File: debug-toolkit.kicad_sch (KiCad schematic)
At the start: 130 parts, among them J1 USB-C_USB4105-GF-A, J2 PinHeader_Shrouded_2x5_P2mm_D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, J3 PinHeader_2x8_P2.54mm_Drill1mm, J4 PinHeader_1x2_P2.54mm_Drill1.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, J5 PinHeader_1x2_P1.27mm_Drill0.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, J6 PinHeader_1x4_P2.54mm_Drill1.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, Q1 NX3008CBKV, Q2 NX3008CBKV, Q3 BC807-25W, Q4 SSM3K15ACT, Q5 SSM3K15ACT, Q6 SSM3K15ACT, Q7 SSM3K15ACT, SW1_A1 PinHeader_1x3_P2.54mm_Drill1.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, SW1_B1 PinHeader_1x3_P2.54mm_Drill1.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, SW2 PinHeader_2x3_P2.54mm_Drill1mm, U1 FT4232H_VQFN, U10 74LVC2T45_SOT833, U11 NTS0302JKZ, U12 TLV70033_SC70, U13 74HC00_DHVQFN, U14 TLV70018_SC70, U15 TS5A3359_VSSOP, U16 TS5A3359_VSSOP, U2 SN74LVC1T45_SOT-5X3, U3 SN74LVC1T45_SOT-5X3, U4 TXB0104_UQFN, U5 74LVC2T45_SOT833, U6 74LVC2T45_SOT833, U7 74LVC2T45_SOT833, U8 SN74LVC1T45_SOT-5X3, U9 SN74LVC1T45_SOT-5X3, Y1 Oscillator_SMD_12MHz_ASFLMB

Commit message: Bump revision, change name on PCB and in schematics
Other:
- title: FTDI Toolkit -> Debug Toolkit
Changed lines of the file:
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@@
   (paper "A2")
   (title_block
-    (title "FTDI Toolkit")
+    (title "Debug Toolkit")
     (date "2022-08-03")
-    (rev "1.3.6")
+    (rev "1.3.8")
     (comment 1 "www.antmicro.com")
     (comment 2 "Antmicro Ltd.")

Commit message: [#57618] Perform globlib
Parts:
- 1V8_A1, 1V8_B1, 3V3_A1, 3V3_B1, 5V0_A1, 5V0_B1, RX_A1, RX_B1, TX_A1, TX_B1, USB1: footprint debug-toolkit-footprints:LED_0603_1608Metric_G -> antmicro-footprints:LED_0603_1608Metric_G; symbol debug-toolkit:LED_G_0603_LG_L29K-G2J1-24-Z -> antmicroLEDIndicationDiscrete:LED_G_0603_LG_L29K-G2J1-24-Z
- C1, C2, C36, C5, C6: footprint debug-toolkit-footprints:C_0603_1608Metric -> antmicro-footprints:C_0603_1608Metric; symbol debug-toolkit:C_1u_0603 -> antmicroCapacitors0603:C_1u_0603
- C11, C23, C27, C33: footprint debug-toolkit-footprints:C_0402_1005Metric -> antmicro-footprints:C_0402_1005Metric; symbol debug-toolkit:C_4u7_0402 -> antmicroCapacitors0402:C_4u7_0402
- C3: footprint debug-toolkit-footprints:C_0402_1005Metric -> antmicro-footprints:C_0402_1005Metric; symbol debug-toolkit:C_10n_0402 -> antmicroCapacitors0402:C_10n_0402
- D1: footprint debug-toolkit-footprints:SOT-723 -> antmicro-footprints:SOT-723; symbol debug-toolkit:TPD2E009_SOT-9X3 -> antmicroTVSDiodes:TPD2E009_SOT-9X3
- D2: footprint debug-toolkit-footprints:USON-14_3.5X1.3X0.5mm_P0.5mm -> antmicro-footprints:USON-14_3.5X1.3X0.5mm_P0.5mm; symbol debug-toolkit:TPD6E05U06RVZR -> antmicroTVSDiodes:TPD6E05U06RVZR
- D3, D4: footprint debug-toolkit-footprints:SOD-523 -> antmicro-footprints:SOD-523; symbol debug-toolkit:BAT54-02V-G3-08 -> antmicroDiodesRectifiersSingle:BAT54-02V-G3-08
- FB1, FB2: footprint debug-toolkit-footprints:FB_0402_1005Metric -> antmicro-footprints:FB_0402_1005Metric; symbol debug-toolkit:FB_600Z_0.3A_0402 -> antmicroFerriteBeadsandChips:FB_600Z_0.3A_Murata-BLM15AG_0402
- J1: footprint debug-toolkit-footprints:GCT_USB4105-GF-A -> antmicro-footprints:USB-C_Receptacle_GCT_USB4105-GF-A; symbol debug-toolkit:USB-C_USB4105-GF-A -> antmicroUSBConnectors:USB-C_GCT_USB4105-GF-A
- J2: footprint debug-toolkit-footprints:IDC-Header_2x05_P1.27_Vertical_SMD_Samtec_SHF-105-01-X-D-SM -> antmicro-footprints:PinHeader_2x5_P1.27mm_SMD_Shrouded; symbol debug-toolkit:PinHeader_Shrouded_2x5_P2mm_Drill0.71mm -> antmicroGenericPinHeaders:PinHeader_2x5_P1.27mm_SMD_Shrouded
- J3: footprint debug-toolkit-footprints:PinHeader_2x8_P2.54mm_Drill1mm -> antmicro-footprints:PinHeader_2x8_P2.54mm_Drill1mm; symbol debug-toolkit:PinHeader_2x8_P2.54mm_Drill1mm -> antmicroGenericPinHeaders:PinHeader_2x8_P2.54mm_Drill1mm
- J4: footprint debug-toolkit-footprints:PinHeader_1x2_P2.54mm_Drill1.02mm -> antmicro-footprints:PinHeader_1x2_P2.54mm_Drill1.02mm; symbol debug-toolkit:PinHeader_1x2_P2.54mm_Drill1.02mm -> antmicroGenericPinHeaders:PinHeader_1x2_P2.54mm_Drill1.02mm
- J5: footprint debug-toolkit-footprints:PinHeader_1x2_P1.27mm_Drill0.7mm -> antmicro-footprints:PinHeader_1x2_P1.27mm_Drill0.7mm; symbol debug-toolkit:PinHeader_1x2_P1.27mm_Drill0.7mm -> antmicroGenericPinHeaders:PinHeader_1x2_P1.27mm_Drill0.7mm
- J6: footprint debug-toolkit-footprints:PinHeader_1x4_P2.54mm_Drill1.02mm -> antmicro-footprints:PinHeader_1x4_P2.54mm_Drill1.1mm; symbol debug-toolkit:PinHeader_1x4_P2.54mm_Drill1.1mm -> antmicroGenericPinHeaders:PinHeader_1x4_P2.54mm_Drill1.1mm
- L1, L2: footprint debug-toolkit-footprints:FB_0603_1608Metric -> antmicro-footprints:FB_0603_1608Metric; symbol debug-toolkit:FB_120Z_2A_0603 -> antmicroFerriteBeadsandChips:FB_120Z_2A_Murata-BLM18PG_0603
- N1: footprint debug-toolkit-footprints:antmicro-logo_scaled_12mm -> antmicro-footprints:antmicro-logo; symbol debug-toolkit:antmicro_logo -> antmicroMechanicalParts:antmicro_logo
- N2: footprint debug-toolkit-footprints:oshw-logo -> antmicro-footprints:oshw-logo; symbol debug-toolkit:oshw_logo -> antmicroMechanicalParts:oshw_logo
- Q1, Q2: footprint debug-toolkit-footprints:SOT-666 -> antmicro-footprints:SOT-666; symbol debug-toolkit:NX3008CBKV -> antmicroTransistorsFETsMOSFETsArrays:NX3008CBKV
- Q3: footprint debug-toolkit-footprints:SOT-323 -> antmicro-footprints:SOT-323; symbol debug-toolkit:BC807-25W -> antmicroTransistorsBipolarSingle:BC807-25W
- Q4, Q5, Q6, Q7: footprint debug-toolkit-footprints:CST3-3 -> antmicro-footprints:CST3-3; symbol debug-toolkit:SSM3K15ACT -> antmicroTransistorsFETsMOSFETsSingle:SSM3K15ACT
- R1, R11, R12, R13, R14, R15, R18, R3, R34, R35, R36, R6, R7, R8: footprint debug-toolkit-footprints:R_0402_1005Metric -> antmicro-footprints:R_0402_1005Metric; symbol debug-toolkit:R_220R_0402 -> antmicroResistors0402:R_220R_0402
- R10, R31, R37, R38: footprint debug-toolkit-footprints:R_0201 -> antmicro-footprints:R_0201; symbol debug-toolkit:R_100k_0201 -> antmicroResistorsmisc:R_100k_0201
- R16, R17, R22, R25, R26, R27, R30, R32, R33, R4, R5: footprint debug-toolkit-footprints:R_0402_1005Metric -> antmicro-footprints:R_0402_1005Metric; symbol debug-toolkit:R_10k_0402 -> antmicroResistors0402:R_10k_0402
- R19, R28: footprint debug-toolkit-footprints:R_0402_1005Metric -> antmicro-footprints:R_0402_1005Metric; symbol debug-toolkit:R_510R_0402 -> antmicroResistors0402:R_510R_0402
- R2: footprint debug-toolkit-footprints:R_0402_1005Metric -> antmicro-footprints:R_0402_1005Metric; symbol debug-toolkit:R_470R_0402 -> antmicroResistors0402:R_470R_0402
- R20, R24: footprint debug-toolkit-footprints:R_0402_1005Metric -> antmicro-footprints:R_0402_1005Metric; symbol debug-toolkit:R_1k_0402 -> antmicroResistors0402:R_1k_0402
- R21: footprint debug-toolkit-footprints:R_0402_1005Metric -> antmicro-footprints:R_0402_1005Metric; symbol debug-toolkit:R_4k7_0402 -> antmicroResistors0402:R_4k7_0402
- R23, R29: footprint debug-toolkit-footprints:R_0402_1005Metric -> antmicro-footprints:R_0402_1005Metric; symbol debug-toolkit:R_56k_0402 -> antmicroResistors0402:R_56k_0402
- R9: footprint debug-toolkit-footprints:R_0402_1005Metric -> antmicro-footprints:R_0402_1005Metric; symbol debug-toolkit:R_12k_0402 -> antmicroResistors0402:R_12k_0402
- SW1_A1, SW1_B1: footprint debug-toolkit-footprints:PinHeader_1x3_P2.54_Drill1.1mm -> antmicro-footprints:PinHeader_1x3_P2.54mm_Drill1.1mm; symbol debug-toolkit:PinHeader_1x3_P2.54mm_Drill1.1mm -> antmicroGenericPinHeaders:PinHeader_1x3_P2.54mm_Drill1.1mm
- SW2: footprint debug-toolkit-footprints:PinHeader_2x3_P2.54mm_Drill1mm -> antmicro-footprints:PinHeader_2x3_P2.54mm_Drill1.1mm; symbol debug-toolkit:PinHeader_2x3_P2.54mm_Drill1mm -> antmicroGenericPinHeaders:PinHeader_2x3_P2.54mm_Drill1.1mm
- U1: footprint debug-toolkit-footprints:QFN-56-1EP_8x8mm_P0.5mm -> antmicro-footprints:QFN-56-1EP_8x8mm_P0.5mm; symbol debug-toolkit:FT4232H_VQFN -> antmicroInterfaceControllers:FT4232H_VQFN
- U10, U5, U6, U7: footprint debug-toolkit-footprints:XSON-8_1x1.95mm_P0.5mm -> antmicro-footprints:XSON-8_1x1.95mm_P0.5mm; symbol debug-toolkit:74LVC2T45_SOT833 -> antmicroLogicTranslatorsLevelShifters:74LVC2T45_SOT833
- U11: footprint debug-toolkit-footprints:X2SON8_1.4x1x0.32mm_P0.35mm -> antmicro-footprints:X2SON8_1.4x1x0.32mm_P0.35mm; symbol debug-toolkit:NTS0302JKZ -> antmicroLogicTranslatorsLevelShifters:NTS0302JKZ
- U12: footprint debug-toolkit-footprints:SC-70-5 -> antmicro-footprints:SC-70-5; symbol debug-toolkit:TLV70033_SC70 -> antmicroPMICVoltageRegulatorsLinear:TLV70033_SC70
- U13: footprint debug-toolkit-footprints:DHVQFN-14_1EP_2.5x3mm -> antmicro-footprints:DHVQFN-14-1EP_2.5x3mm; symbol debug-toolkit:74HC00_DHVQFN -> antmicroLogicGatesandInverters:74HC00_DHVQFN
- U14: footprint debug-toolkit-footprints:SC-70-5 -> antmicro-footprints:SC-70-5; symbol debug-toolkit:TLV70018_SC70 -> antmicroPMICVoltageRegulatorsLinear:TLV70018_SC70
- U15, U16: footprint debug-toolkit-footprints:VSSOP-8_2.3x2mm_P0.5mm -> antmicro-footprints:VSSOP-8_2.3x2mm_P0.5mm; symbol debug-toolkit:TS5A3359_VSSOP -> antmicroInterfaceAnalogSwitchesMultiplexersDemultiplexers:TS5A3359_VSSOP
- U2, U3, U8, U9: footprint debug-toolkit-footprints:SOT-553-6 -> antmicro-footprints:SOT-553-6; symbol debug-toolkit:SN74LVC1T45_SOT-5X3 -> antmicroLogicTranslatorsLevelShifters:SN74LVC1T45_SOT-5X3
- U4: footprint debug-toolkit-footprints:UQFN-12_2x1.7mm_P0.4mm_Texas_RUT -> antmicro-footprints:UQFN-12_2x1.7mm_P0.4mm_Texas_RUT; symbol debug-toolkit:TXB0104_UQFN -> antmicroLogicTranslatorsLevelShifters:TXB0104_UQFN
- Y1: footprint debug-toolkit-footprints:Oscillator_SMD_Abracon_ASFLMB_5x3.2x0.85mm -> antmicro-footprints:Oscillator_SMD_Abracon_ASFLMB_5x3.2x0.85mm; symbol debug-toolkit:Oscillator_SMD_12MHz_ASFLMB -> antmicroOscillators:Oscillator_12MHz_ASFLMB

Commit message: [#57618] Update symbols from global lib
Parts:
- 1V8_A1, 1V8_B1, 3V3_A1, 3V3_B1, 5V0_A1, 5V0_B1, RX_A1, RX_B1, TX_A1, TX_B1, USB1: Color (none) -> Green; Manufacturer Osram -> OSRAM
- FB1, FB2: value FB_600Z_0.3A_0402 -> FB_600Z_0.3A_Murata-BLM15AG_0402; Val (none) -> 600Z/0.3A
- J1: value USB-C_USB4105-GF-A -> USB-C_GCT_USB4105-GF-A; VSD_Class (none) -> USB-C
- J2: value PinHeader_Shrouded_2x5_P2mm_Drill0.71mm -> PinHeader_2x5_P1.27mm_SMD_Shrouded
- J3: Manufacturer Wurth -> Würth Elektronik
- J4: Manufacturer Harwin -> Molex
- J5: Manufacturer Multicomp -> Multicomp Pro
- L1, L2: value FB_120Z_2A_0603 -> FB_120Z_2A_Murata-BLM18PG_0603; Val (none) -> 120Z/2A
- N1, N2: Manufacturer None -> (none); now left out of the parts list
- Q3: MPN SBC807-25WT1G -> SBC807-40WT1G
- Q4, Q5, Q6, Q7: MPN SSM3K15ACT,L3F -> SSM3K15ACT,L3F
- SW1_A1, SW1_B1: VSD_class (none) -> IO Header
- SW2: value PinHeader_2x3_P2.54mm_Drill1mm -> PinHeader_2x3_P2.54mm_Drill1.1mm; Manufacturer Wurth -> Würth Elektronik
- U1: Manufacturer FTDI -> FTDI Chip
- Y1: value Oscillator_SMD_12MHz_ASFLMB -> Oscillator_12MHz_ASFLMB; Val (none) -> 12 MHz
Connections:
- net 3V3_FT: now also SW2.3, SW2.4; no longer SW2.2, SW2.5
- net MPSSE_B: now also SW2.5; no longer SW2.3
- net SWD_EN: now also SW2.2; no longer SW2.4
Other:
- moved on the sheet: 1V8_A1, 1V8_B1, 3V3_A1, 3V3_B1, 5V0_A1, 5V0_B1, C1, C10, C11, C12, C13, C14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

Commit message: [#57618] Update C_100n_16V_0402 to global lib
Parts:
- C10, C12, C13, C14, C15, C16, C17, C18, C19, C20, C21, C22, C24, C25, C26, C28, C29, C30, C31, C32, C34, C35, C4, C7, C8, C9: value C_100n_16V_0402 -> C_100n_16V_X7R_0402; footprint debug-toolkit-footprints:C_0402_1005Metric -> antmicro-footprints:C_0402_1005Metric; symbol debug-toolkit:C_100n_16V_0402 -> antmicroCapacitors0402:C_100n_16V_X7R_0402; Dielectric (none) -> X7R; MPN MC0402B104K160CT -> C0402C104J4RAC7411; Manufacturer Multicomp -> KEMET; Voltage (none) -> 16V

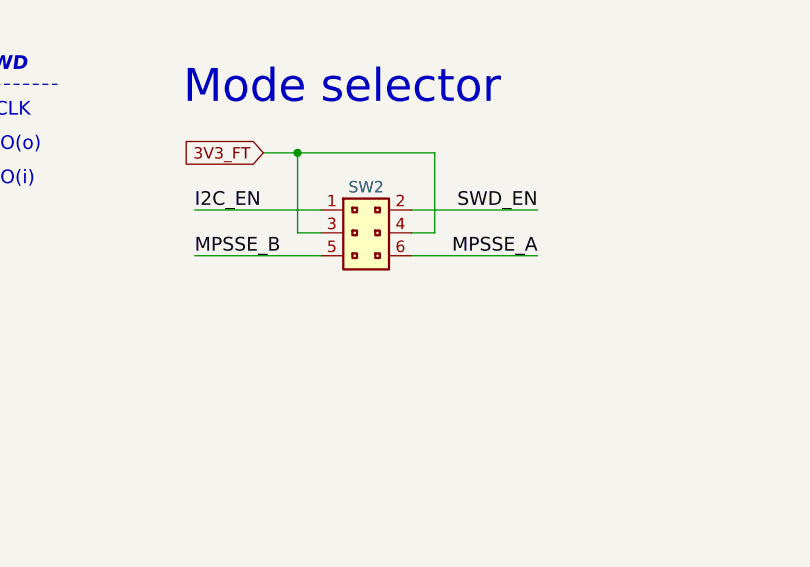
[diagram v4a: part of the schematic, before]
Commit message: [#57618] Update SW2 diameter and MPN
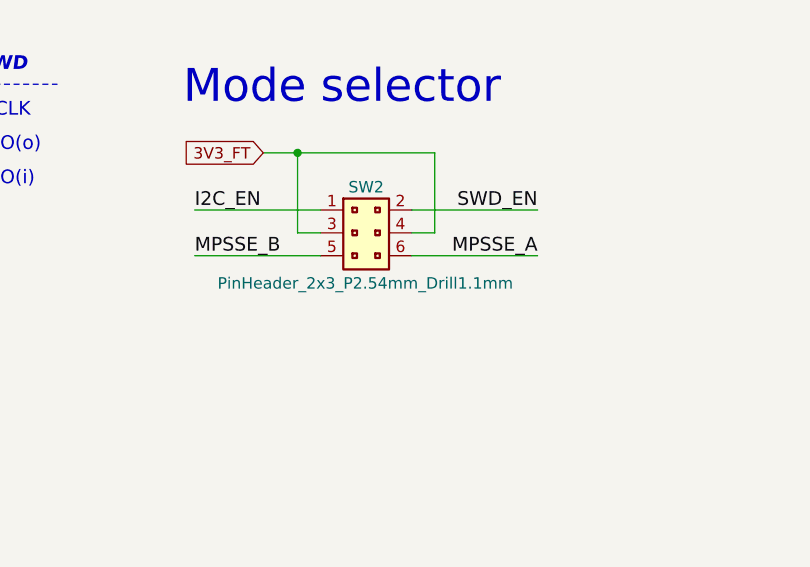
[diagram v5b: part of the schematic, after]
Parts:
- SW2: MPN 61000621121 -> 61300621121
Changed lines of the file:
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@@
       (effects (font (size 1.27 1.27) (thickness 0.15)))
     )
-    (property "Value" "PinHeader_2x3_P2.54mm_Drill1.1mm" (at 173.99 341.63 0)
-      (effects (font (size 1.27 1.27) (thickness 0.15)) (justify left bottom) hide)
+    (property "Value" "PinHeader_2x3_P2.54mm_Drill1.1mm" (at 137.16 342.9 0)
+      (effects (font (size 1.27 1.27) (thickness 0.15)) (justify left bottom))
     )
     (property "Footprint" "antmicro-footprints:PinHeader_2x3_P2.54mm_Drill1.1mm" (at 173.99 344.17 0)
@@
       (effects (font (size 1.27 1.27) (thickness 0.15)) (justify left bottom) hide)
     )
-    (property "MPN" "61000621121" (at 173.99 351.79 0)
+    (property "MPN" "61300621121" (at 173.99 351.79 0)
       (effects (font (size 1.27 1.27) (thickness 0.15)) (justify left bottom) hide)
     )

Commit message: [#57618] Update symbols
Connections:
- net 3V3_FT: now also D3.2 (A); no longer D3.1
- net SDA: now also D4.1 (C); no longer D4.2
- net at C33.2, R34.1, U11.1 (VCC_A): now also D3.1 (C); no longer D3.2
- net at U7.7 (1B): now also D4.2 (A); no longer D4.1
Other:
- moved on the sheet: R10, R31, R37, R38

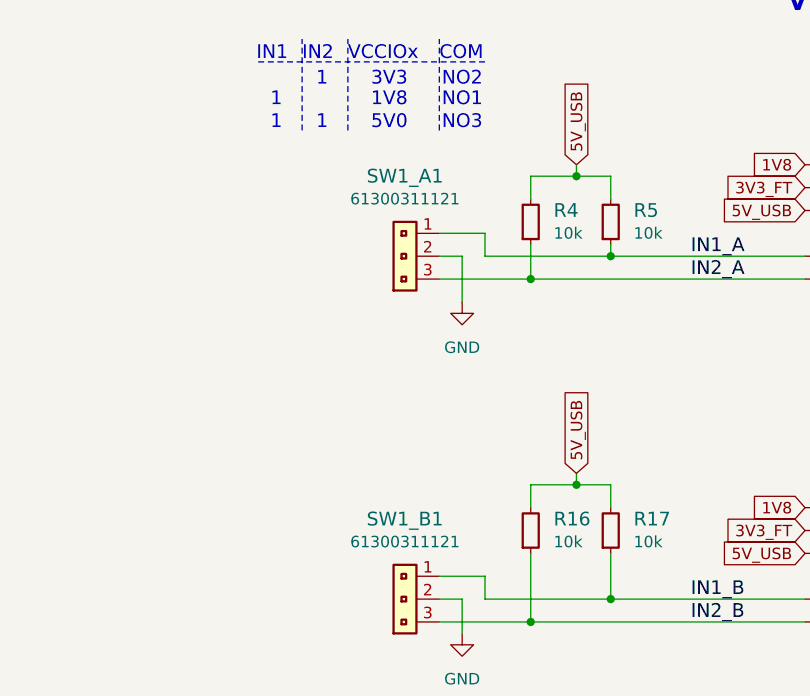
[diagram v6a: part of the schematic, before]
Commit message: Rename SW1 to J1
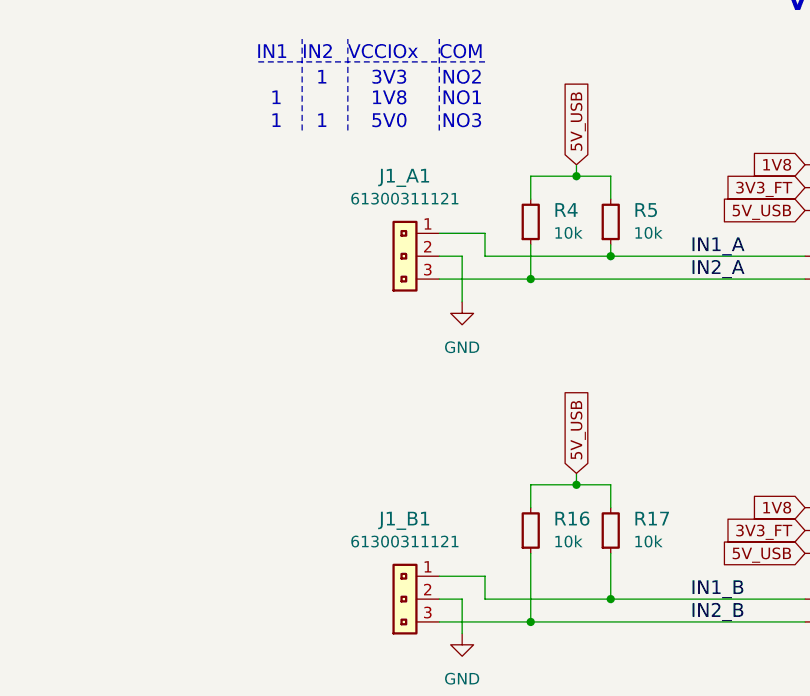
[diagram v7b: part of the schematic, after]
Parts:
- renumbered SW1_A1 to J1_A1, SW1_B1 to J1_B1
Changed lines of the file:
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@@
   (symbol (lib_id "antmicroGenericPinHeaders:PinHeader_1x3_P2.54mm_Drill1.1mm") (at 309.88 91.44 0) (mirror y) (unit 1)
     (in_bom yes) (on_board yes) (dnp no) (fields_autoplaced)
-    (property "Reference" "SW1_B1" (at 306.07 85.09 0)
+    (property "Reference" "J1_B1" (at 306.07 85.09 0)
       (effects (font (size 1.524 1.524)))
     )
@@
       (project "debug-toolkit"
         (path "/dd9af27c-a67f-40d3-942b-1892dec86b34"
-          (reference "SW1_B1") (unit 1)
+          (reference "J1_B1") (unit 1)
         )
       )
@@
   (symbol (lib_id "antmicroGenericPinHeaders:PinHeader_1x3_P2.54mm_Drill1.1mm") (at 309.88 53.34 0) (mirror y) (unit 1)
     (in_bom yes) (on_board yes) (dnp no) (fields_autoplaced)
-    (property "Reference" "SW1_A1" (at 306.07 46.99 0)
+    (property "Reference" "J1_A1" (at 306.07 46.99 0)
       (effects (font (size 1.524 1.524)))
     )
@@
       (project "debug-toolkit"
         (path "/dd9af27c-a67f-40d3-942b-1892dec86b34"
-          (reference "SW1_A1") (unit 1)
+          (reference "J1_A1") (unit 1)
         )
       )

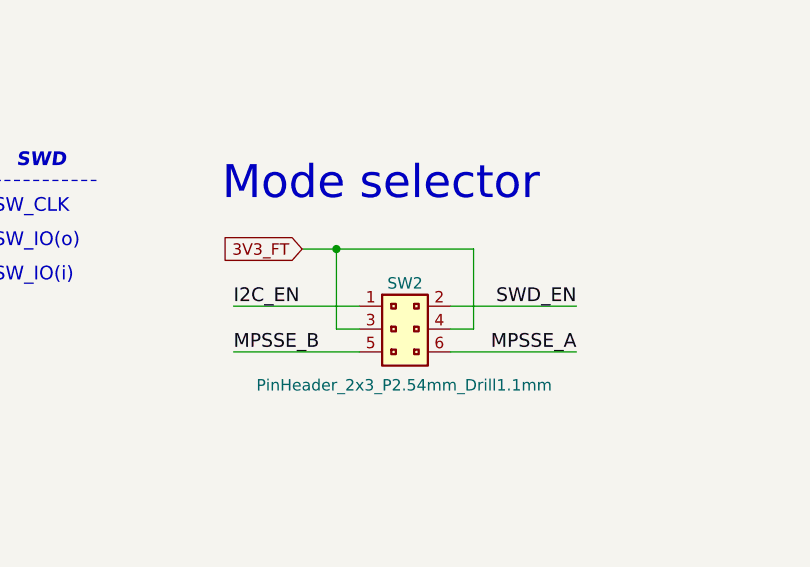
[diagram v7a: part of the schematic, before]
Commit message: Rename SW2 to J7
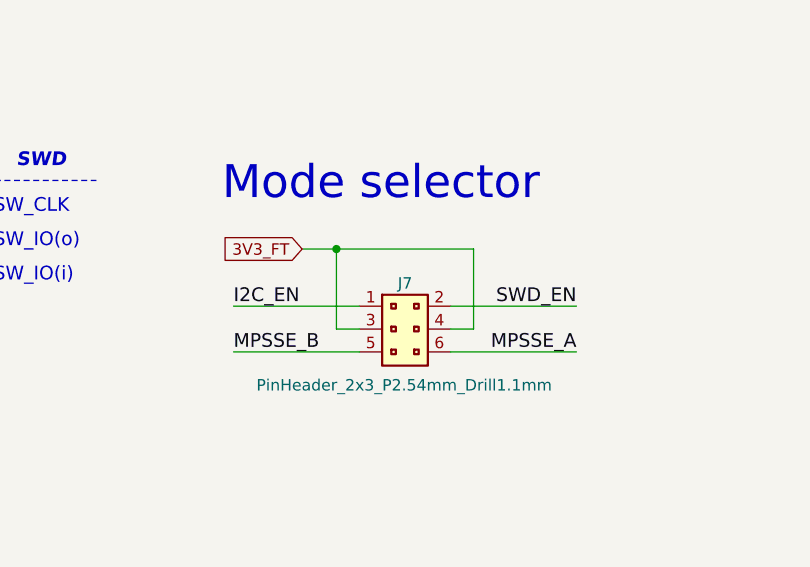
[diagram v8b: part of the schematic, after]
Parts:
- renumbered SW2 to J7
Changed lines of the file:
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@@
   (symbol (lib_id "antmicroGenericPinHeaders:PinHeader_2x3_P2.54mm_Drill1.1mm") (at 148.59 334.01 0) (unit 1)
     (in_bom yes) (on_board yes) (dnp no)
-    (property "Reference" "SW2" (at 153.67 331.47 0)
+    (property "Reference" "J7" (at 153.67 331.47 0)
       (effects (font (size 1.27 1.27) (thickness 0.15)))
     )
@@
       (project "debug-toolkit"
         (path "/dd9af27c-a67f-40d3-942b-1892dec86b34"
-          (reference "SW2") (unit 1)
+          (reference "J7") (unit 1)
         )
       )
